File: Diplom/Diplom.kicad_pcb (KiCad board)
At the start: 2 copper layers, 100 x 100 mm, 84 parts, among them IC1 E22-900T22D, J2 Conn_01x04_Pin, Q1 SI2301, SW1 SW_Push, SW2 SW_Push, U2 BME280, U3 W25Q32JVSS, U4 SPV1040, U5 DW01A, U6 STM32F411CEUx, Y3 ABM3-25.000MHz-D2Y-T, Y4 KX-327NHT, Y5 Crystal

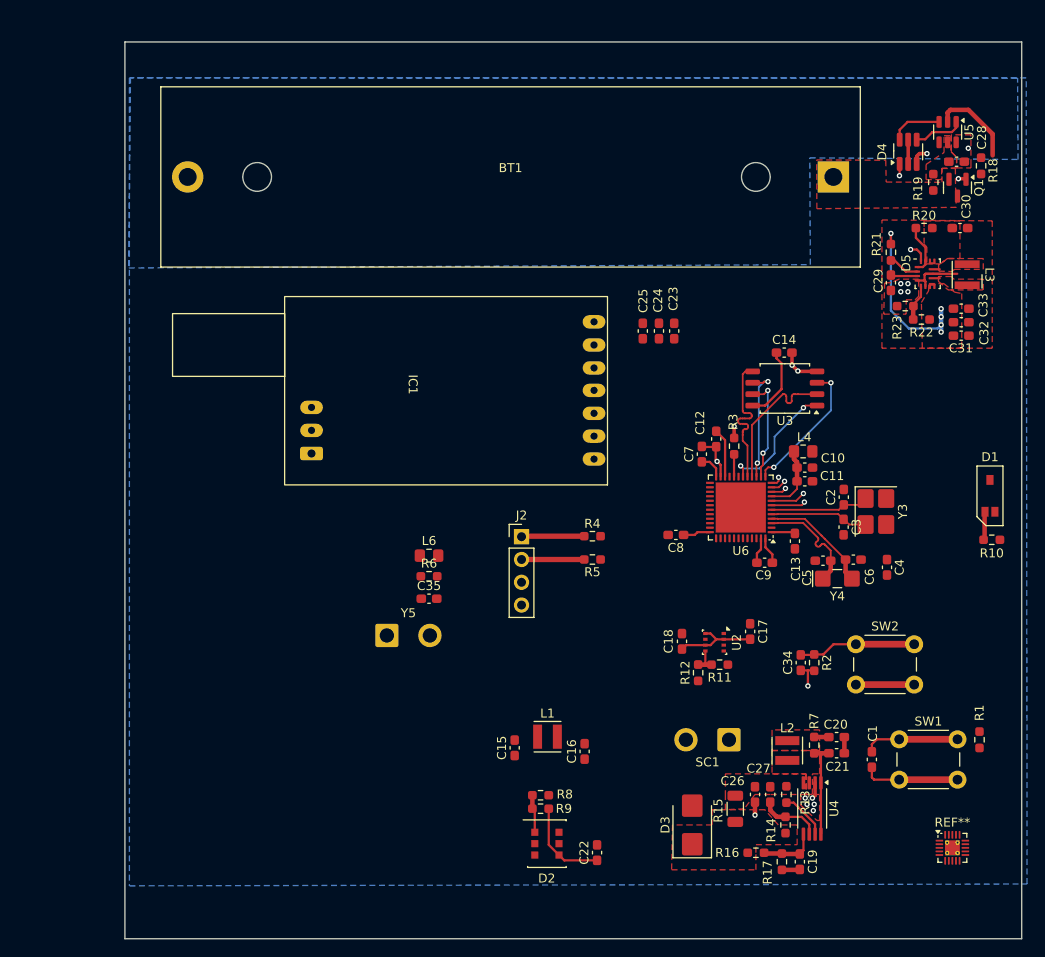
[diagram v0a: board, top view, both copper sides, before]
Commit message: version 2.0 fix buttons, roots, tighten dimension
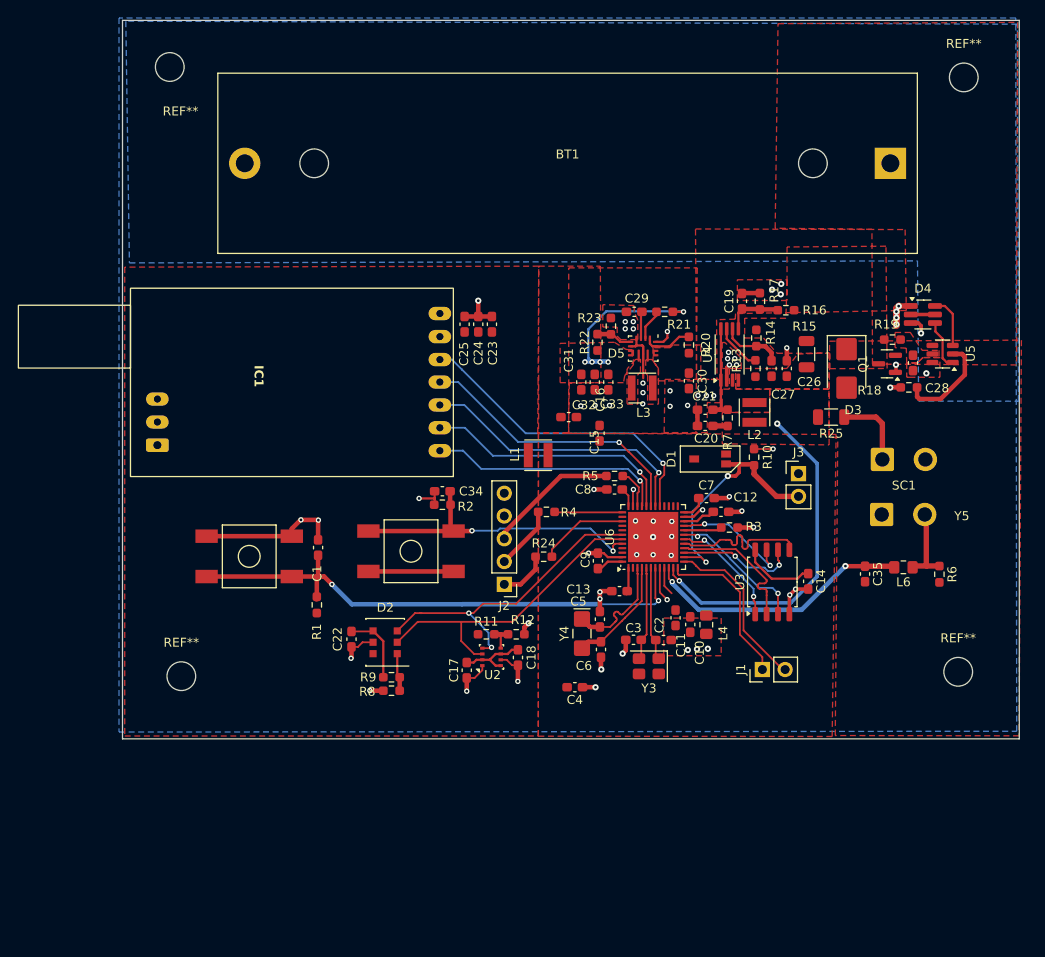
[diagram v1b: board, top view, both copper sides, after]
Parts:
- removed the REF** at (143.6, 119.0)
- added J1: Conn_01x02_Pin, Connector_PinHeader_2.54mm:PinHeader_1x02_P2.54mm_Vertical, F.Cu at (122.4, 99.1)
- added J3: Conn_01x02_Pin, Connector_PinHeader_2.54mm:PinHeader_1x02_P2.54mm_Vertical, F.Cu at (126.4, 77.2)
- added R24: 22 Ом, Resistor_SMD:R_0603_1608Metric_Pad0.98x0.95mm_HandSolder, F.Cu at (98.0, 86.5)
- added R25: 240 мОм, Resistor_SMD:R_1206_3216Metric, F.Cu at (130.1, 70.9)
- added REF**: MountingHole_3.2mm_M3_DIN965, MountingHole:MountingHole_3.2mm_M3_DIN965, F.Cu at (144.8, 33.0)
- added REF**: MountingHole_3.2mm_M3_DIN965, MountingHole:MountingHole_3.2mm_M3_DIN965, F.Cu at (57.6, 99.8)
- added REF**: MountingHole_3.2mm_M3_DIN965, MountingHole:MountingHole_3.2mm_M3_DIN965, F.Cu at (144.2, 99.3)
- added REF**: MountingHole_3.2mm_M3_DIN965, MountingHole:MountingHole_3.2mm_M3_DIN965, F.Cu at (56.3, 31.9)
- J2: value Conn_01x04_Pin -> Conn_01x05_Pin; footprint Connector_PinHeader_2.54mm:PinHeader_1x04_P2.54mm_Vertical -> Connector_PinHeader_2.54mm:PinHeader_1x05_P2.54mm_Vertical
- SW1, SW2: footprint Button_Switch_THT:SW_PUSH_6mm_H7.3mm -> Diplom:FSM8JSMATR
- Y3: footprint Crystal:Crystal_SMD_3225-4Pin_3.2x2.5mm_HandSoldering -> Crystal:Crystal_SMD_3225-4Pin_3.2x2.5mm
- moved R1 75.4 mm to (72.7, 91.9), turned to 90 degrees
- moved SW1 75.3 mm to (65.2, 86.5), turned to 90 degrees
- moved C1 66.1 mm to (72.8, 85.5), turned to 90 degrees
- moved C19 62.8 mm to (120.1, 58.0), turned to 90 degrees
- moved R17 62.5 mm to (122.1, 58.0), turned to -90 degrees
- moved R16 60.6 mm to (125.0, 59.0), turned to 0 degrees
- moved R6 56.9 mm to (142.1, 88.5), turned to -90 degrees
- moved Y5 56.8 mm to (135.7, 81.8)
- moved R14 54.4 mm to (121.7, 62.1), turned to 90 degrees
- moved D3 53.7 mm to (131.8, 65.5), turned to -90 degrees
- moved L6 52.9 mm to (138.1, 87.7), turned to 180 degrees
- moved U4 51.5 mm to (118.7, 63.9), turned to 90 degrees
- moved R15 51.3 mm to (127.3, 63.9), turned to 90 degrees
- moved SW2 50.7 mm to (83.2, 85.9), turned to -90 degrees
- moved C35 48.7 mm to (133.8, 88.4), turned to -90 degrees
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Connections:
- C14 pad 1: +3V3 -> VDD_MCU
- C20 pad 1: Net-(SC1-+) -> /Power/PV_CURRENT
- C4 pad 1: +3V3 -> VDD_MCU
- D1 pad 3: +3V3 -> VDD_MCU
- J2 pad 3: GND -> Net-(J2-Pin_3)
- J2 pad 4: +3V3 -> GND
- L2 pad 1: Net-(SC1-+) -> /Power/PV_CURRENT
- R4 pad 2: Net-(J2-Pin_1) -> Net-(J2-Pin_2)
- R5 pad 2: Net-(J2-Pin_2) -> Net-(J2-Pin_3)
- R7 pad 1: Net-(SC1-+) -> /Power/PV_CURRENT
- U3 pad 8: +3V3 -> VDD_MCU
- U6 pad 12: /MCU/TEMT6000 -> /MCU/USART2_TX
- U6 pad 13: /MCU/N_WP -> /MCU/USART2_RX
- U6 pad 14: /MCU/N_HOLD -> /MCU/TEMT6000
- U6 pad 19: unconnected-(U6-PB1-Pad19) -> /MCU/N_WP
- U6 pad 21: unconnected-(U6-PB10-Pad21) -> /MCU/N_HOLD
- U6 pad 27: /MCU/M1_LORA -> unconnected-(U6-PB14-Pad27)
- U6 pad 28: /MCU/M0_LORA -> unconnected-(U6-PB15-Pad28)
- U6 pad 32: unconnected-(U6-PA11-Pad32) -> /MCU/M0_LORA
- U6 pad 33: unconnected-(U6-PA12-Pad33) -> /MCU/M1_LORA
- U6 pad 39: unconnected-(U6-PB3-Pad39) -> /MCU/SYS_SWO
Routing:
- net /MCU/NRST: track 14.5 -> 60.6 mm, vias 1 -> 2
- net GND: track 49.4 -> 92.6 mm, vias 19 -> 69
- net /MCU/PV_CURRENT: track 1.74 -> 38.2 mm, vias 1 -> 2
- net /MCU/I2C1_SCL: track 0.00 -> 35.7 mm, vias 0 -> 2
- net /MCU/I2C1_SDA: track 0.00 -> 34.9 mm
- net /MCU/AUX_LORA: track 0.00 -> 34.7 mm, vias 0 -> 1
- net /MCU/USART1_TX_LORA: track 0.00 -> 31.4 mm, vias 0 -> 1
- net /MCU/USART1_RX_LORA: track 0.00 -> 31.4 mm, vias 0 -> 1
- net /MCU/M0_LORA: track 0.00 -> 28.5 mm, vias 0 -> 1
- net /MCU/PIEZO: track 1.72 -> 29.8 mm, vias 1 -> 2
- net /MCU/M1_LORA: track 0.00 -> 26.7 mm, vias 0 -> 1
- net /MCU/TEMT6000: track 4.47 -> 27.2 mm, vias 1 -> 2
- net /MCU/BOOT0: track 13.1 -> 34.7 mm, vias 0 -> 2
- net /MCU/USART2_RX: track 0.00 -> 19.0 mm
- net /MCU/USART2_TX: track 0.00 -> 18.1 mm
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- added copper zone on F.Cu, net /Power/PV_CURRENT
- added copper zone on F.Cu, net VDD_MCU
- removed copper zone on F.Cu, net Net-(SC1-+)
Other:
- board size 100 x 100 mm -> 100 x 80.1 mm

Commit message: Исправил место под кварц 25МГц, заменил батарею на пакет, перевернул лору. Сырая компоновка без разводки
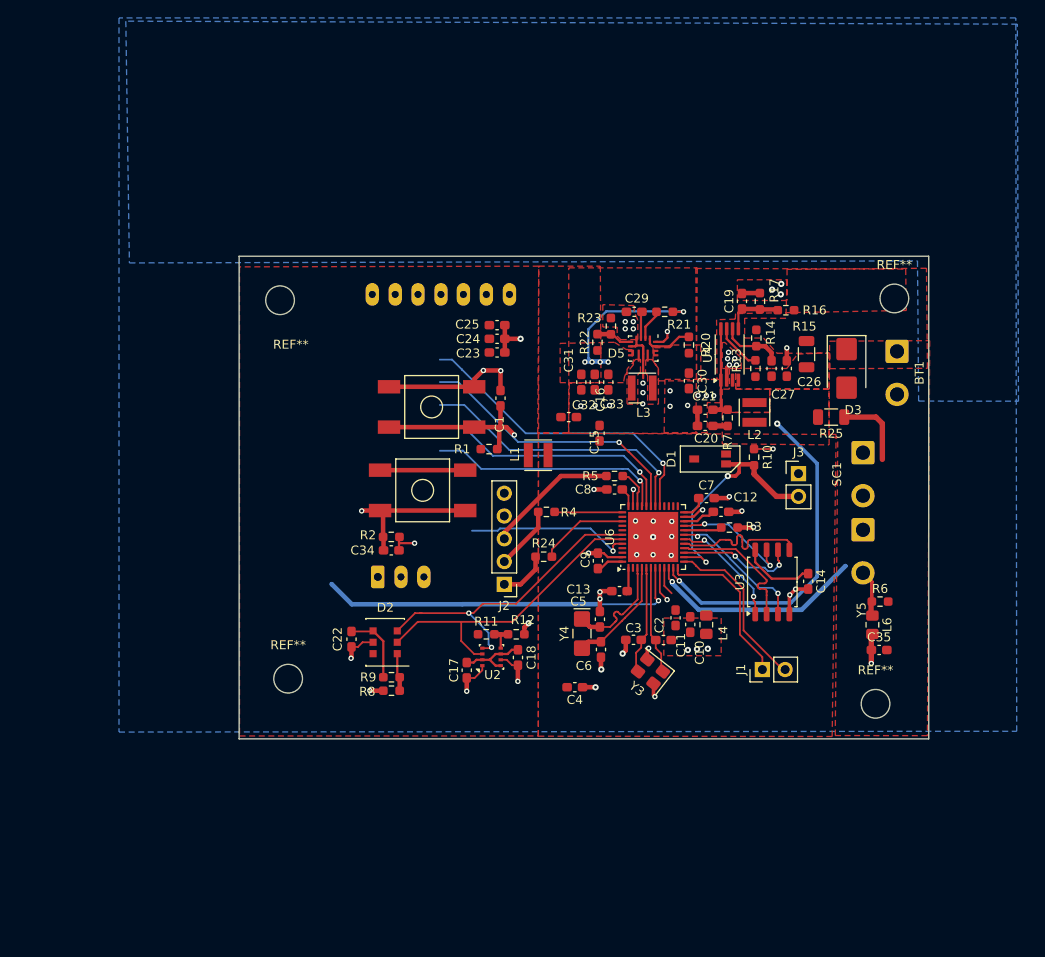
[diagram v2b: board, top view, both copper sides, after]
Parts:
- removed C28: 0,1 мкФ 25 В, Capacitor_SMD:C_0603_1608Metric_Pad1.08x0.95mm_HandSolder
- removed D4: FS8205A, Package_TO_SOT_SMD:SOT-23-6_Handsoldering
- removed Q1: SI2301, Package_TO_SOT_SMD:SOT-23
- removed R18: 1 кОм, Resistor_SMD:R_0603_1608Metric_Pad0.98x0.95mm_HandSolder
- removed R19: 100 Ом, Resistor_SMD:R_0603_1608Metric_Pad0.98x0.95mm_HandSolder
- removed U5: DW01A, Package_TO_SOT_SMD:SOT-23-6
- BT1: footprint Battery:BatteryHolder_MPD_BH-18650-PC2 -> Connector_Wire:SolderWire-0.75sqmm_1x02_P4.8mm_D1.25mm_OD2.3mm
- IC1: moved to B.Cu
- Y3: value ABM3-25.000MHz-D2Y-T -> Crystal_GND24
- moved REF** 28.8 mm to (68.6, 57.9)
- moved C1 26.3 mm to (93.2, 68.8)
- moved SW1 26.3 mm to (85.5, 69.8)
- moved R1 25.9 mm to (91.9, 74.5), turned to 0 degrees
- moved REF** 25.8 mm to (137.1, 57.7)
- moved BT1 21.0 mm to (137.4, 63.6), turned to -90 degrees
- moved IC1 16.3 mm to (87.0, 72.0), turned to 180 degrees
- moved REF** 11.9 mm to (69.5, 100.1)
- moved REF** 9.89 mm to (135.0, 102.9)
- moved C34 8.71 mm to (81.0, 85.8), turned to 180 degrees
- moved C35 8.62 mm to (135.4, 96.9), turned to 0 degrees
- moved R6 7.29 mm to (135.5, 91.5), turned to 0 degrees
- moved L6 7.28 mm to (134.7, 94.1), turned to -90 degrees
- moved SW2 6.91 mm to (84.5, 79.1), turned to 90 degrees
- moved R2 6.74 mm to (81.0, 84.3), turned to 0 degrees
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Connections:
- BT1 pad 1: Net-(BT1-+) -> /Power/VBAT+
- BT1 pad 2: Net-(BT1--) -> GND
- Y3 pad 2: /MCU/OSC_N -> GND
- Y3 pad 3: (no net) -> /MCU/OSC_N
- Y3 pad 4: (no net) -> GND
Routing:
- net Net-(U5-CS): track 11.1 -> 0.00 mm
- net Net-(D4A-G): track 5.87 -> 0.00 mm
- net Net-(D4B-G): track 5.61 -> 0.00 mm
- net Net-(L6-Pad1): track 8.05 -> 5.03 mm
- net Net-(D4A-D-Pad2): track 2.70 -> 0.00 mm
- net GND: track 92.6 -> 90.0 mm, vias 69 -> 65
- net /MCU/PIEZO: track 29.8 -> 27.6 mm
- net Net-(BT1--): track 2.12 -> 0.00 mm, vias 2 -> 0
- net /MCU/OSC_N: track 10.5 -> 12.1 mm
- net /MCU/OSC_P: track 10.5 -> 12.1 mm
- net /MCU/BOOT0: track 34.7 -> 34.2 mm
- removed copper zone on F.Cu, net Net-(BT1-+)
- removed copper zone on B.Cu, net Net-(BT1--)
- removed copper zone on F.Cu, net Net-(BT1--)
- removed copper zone on F.Cu, net Net-(U5-VCC)
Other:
- board size 100 x 80.1 mm -> 76.9 x 53.8 mm

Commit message: corr
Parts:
- removed D1: TEMT6000, Diplom:TEMT6000
- removed R10: 10 кОм, Resistor_SMD:R_0603_1608Metric_Pad0.98x0.95mm_HandSolder
- J3: footprint Connector_PinHeader_2.54mm:PinHeader_1x02_P2.54mm_Vertical -> Connector_PinHeader_2.54mm:PinHeader_1x03_P2.54mm_Vertical
- moved IC1 18.2 mm to (105.0, 74.4), turned to -90 degrees
- moved C1 11.5 mm to (82.8, 63.8), turned to 180 degrees
- moved R1 10.0 mm to (88.5, 65.1), turned to 90 degrees
- moved REF** 9.87 mm to (77.9, 61.2)
- moved C34 9.56 mm to (90.4, 87.6), turned to -90 degrees
- moved R2 8.56 mm to (88.9, 87.6), turned to 90 degrees
- moved REF** 7.90 mm to (77.4, 100.3)
- moved C25 7.82 mm to (92.8, 68.5), turned to 90 degrees
- moved C24 6.48 mm to (94.3, 68.5), turned to 90 degrees
- moved C23 5.65 mm to (95.8, 68.5), turned to 90 degrees
- moved SW2 5.06 mm to (83.7, 84.1), turned to 180 degrees
- moved REF** 4.89 mm to (131.3, 99.7)
- moved C22 4.49 mm to (81.1, 95.8)
- moved R8 4.49 mm to (85.5, 101.5)
- moved D2 4.49 mm to (84.8, 96.1)
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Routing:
- net /MCU/NRST: track 60.3 -> 9.50 mm, vias 2 -> 0
- net /MCU/I2C1_SDA: track 34.9 -> 29.6 mm
- net GND: track 90.0 -> 86.1 mm, vias 65 -> 63
- net /MCU/I2C1_SCL: track 35.7 -> 32.0 mm
- net /MCU/TEMT6000: track 27.2 -> 25.4 mm
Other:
- board size 76.9 x 53.8 mm -> 76.9 x 51.1 mm

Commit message: Add submodule, correction
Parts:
- J1: value Conn_01x02_Pin -> Conn_01x03_Pin; footprint Connector_PinHeader_2.54mm:PinHeader_1x02_P2.54mm_Vertical -> Connector_PinHeader_2.54mm:PinHeader_1x03_P2.54mm_Vertical
- moved J1 2.72 mm to (119.7, 99.1)
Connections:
- J1 pad 1: /MCU/USART2_TX -> GND
- J1 pad 2: /MCU/USART2_RX -> /MCU/USART2_TX
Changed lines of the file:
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@@
 		)
 	)
-	(footprint "Connector_PinHeader_2.54mm:PinHeader_1x02_P2.54mm_Vertical"
+	(footprint "Connector_PinHeader_2.54mm:PinHeader_1x03_P2.54mm_Vertical"
 		(layer "F.Cu")
-		(at 122.38 99.08 90)
-		(descr "Through hole straight pin header, 1x02, 2.54mm pitch, single row")
-		(tags "Through hole pin header THT 1x02 2.54mm single row")
+		(at 119.66 99.08 90)
+		(descr "Through hole straight pin header, 1x03, 2.54mm pitch, single row")
+		(tags "Through hole pin header THT 1x03 2.54mm single row")
 		(property "Reference" "J1"
 			(at 0 -2.38 90)
@@
 			)
 		)
-		(property "Value" "Conn_01x02_Pin"
-			(at 0 4.919999 90)
+		(property "Value" "Conn_01x03_Pin"
+			(at 0 7.46 90)
 			(layer "F.Fab")
 			(effects
@@
 			)
 		)
-		(property "Description" "Generic connector, single row, 01x02, script generated"
+		(property "Description" "Generic connector, single row, 01x03, script generated"
 			(at 0 0 90)
 			(layer "F.Fab")
@@
 		(fp_line
 			(start -1.38 -1.38)
-			(end 0 -1.379999)
-			(stroke
-				(width 0.12)
-				(type solid)
-			)
-			(layer "F.SilkS")
-		)
-		(fp_line
-			(start -1.379999 0)
+			(end 0 -1.38)
+			(stroke
+				(width 0.12)
+				(type solid)
+			)
+			(layer "F.SilkS")
+		)
+		(fp_line
+			(start -1.38 0)
 			(end -1.38 -1.38)
 			(stroke
@@
 		(fp_line
 			(start 1.38 1.27)
-			(end 1.38 3.92)
+			(end 1.38 6.46)
 			(stroke
 				(width 0.12)
@@
 		(fp_line
 			(start -1.38 1.27)
-			(end -1.38 3.92)
-			(stroke
-				(width 0.12)
-				(type solid)
-			)
-			(layer "F.SilkS")
-		)
-		(fp_line
-			(start -1.38 3.92)
-			(end 1.38 3.92)
+			(end -1.38 6.46)
+			(stroke
+				(width 0.12)
+				(type solid)
+			)
+			(layer "F.SilkS")
+		)
+		(fp_line
+			(start -1.38 6.46)
+			(end 1.38 6.46)
 			(stroke
 				(width 0.12)
@@
 		(fp_line
 			(start -1.77 -1.77)
-			(end -1.77 4.32)
-			(stroke
-				(width 0.05)
-				(type solid)
-			)
-			(layer "F.CrtYd")
-		)
-		(fp_line
-			(start 1.77 4.32)
+			(end -1.77 6.85)
+			(stroke
+				(width 0.05)
+				(type solid)
+			)
+			(layer "F.CrtYd")
+		)
+		(fp_line
+			(start 1.77 6.85)
 			(end 1.77 -1.77)
 			(stroke
@@
 		)
 		(fp_line
-			(start -1.77 4.32)
-			(end 1.77 4.32)
+			(start -1.77 6.85)
+			(end 1.77 6.85)
 			(stroke
 				(width 0.05)
@@
 		(fp_line
 			(start 1.27 -1.27)
-			(end 1.27 3.81)
+			(end 1.27 6.35)
 			(stroke
 				(width 0.1)
@@
 		)
 		(fp_line
-			(start 1.27 3.81)
-			(end -1.27 3.81)
-			(stroke
-				(width 0.1)
-				(type solid)
-			)
-			(layer "F.Fab")
-		)
-		(fp_line
-			(start -1.27 3.81)
+			(start 1.27 6.35)
+			(end -1.27 6.35)
+			(stroke
+				(width 0.1)
+				(type solid)
+			)
+			(layer "F.Fab")
+		)
+		(fp_line
+			(start -1.27 6.35)
 			(end -1.27 -0.635)
 			(stroke
@@
 		)
 		(fp_text user "${REFERENCE}"
-			(at 0 1.270001 0)
+			(at 0 2.54 180)
 			(layer "F.Fab")
 			(effects
@@
 			(layers "*.Cu" "*.Mask")
 			(remove_unused_layers no)
-			(net 65 "/MCU/USART2_TX")
+			(net 1 "GND")
 			(pinfunction "Pin_1")
 			(pintype "passive")
@@
 			(layers "*.Cu" "*.Mask")
 			(remove_unused_layers no)
-			(net 57 "/MCU/USART2_RX")
+			(net 65 "/MCU/USART2_TX")
 			(pinfunction "Pin_2")
 			(pintype "passive")
 		)
+		(pad "3" thru_hole circle
+			(at 0 5.08 90)
+			(size 1.7 1.7)
+			(drill 1)
+			(layers "*.Cu" "*.Mask")
+			(remove_unused_layers no)
+			(net 57 "/MCU/USART2_RX")
+			(pinfunction "Pin_3")
+			(pintype "passive")
+		)
 		(embedded_fonts no)
-		(model "${KICAD9_3DMODEL_DIR}/Connector_PinHeader_2.54mm.3dshapes/PinHeader_1x02_P2.54mm_Vertical.step"
+		(model "${KICAD9_3DMODEL_DIR}/Connector_PinHeader_2.54mm.3dshapes/PinHeader_1x03_P2.54mm_Vertical.step"
 			(offset
 				(xyz 0 0 0)
@@
 		(fp_poly
 			(pts
-				(xy -2.099999 -1.750001) (xy -2.1 1.750001) (xy 2.099999 1.750001) (xy 2.1 -1.750001)
-			)
-			(stroke
+				(xy -2.099999 -1.750001) (xy -2.1 1.750002) (xy 2.099999 1.750001) (xy 2.1 -1.750002)
+			)
+			(stroke
